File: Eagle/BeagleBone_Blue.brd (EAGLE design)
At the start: 86.4 x 54.6 mm, 297 parts, among them M1 JST_ZH_2, M2 JST_ZH_2, M3 JST_ZH_2, M4 JST_ZH_2, P10 SCHA5B0200, Q3 MOSFET-N, U1 TPD4S012_DRY_6, U4 TPD4S012_DRY_6, U5 24LC_32AT-I/OT, U6 SN74LVC1G07_DCK_5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

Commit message: Board and schematic consistent
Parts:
- C$1: value (none) -> AVE107M06D16T-F
- moved 6V_REG 207.4 mm to (-47.0, 63.5)
- moved ADC 207.4 mm to (-49.5, 88.9)
- moved BOOT 207.4 mm to (-29.2, 82.5)
- moved C1 207.4 mm to (-81.3, 109.2)
- moved C11 207.4 mm to (-80.0, 73.7)
- moved C13 207.4 mm to (-99.1, 109.2)
- moved C15 207.4 mm to (-104.1, 109.2)
- moved C17 207.4 mm to (-106.7, 109.2)
- moved C19 207.4 mm to (-14.0, 113.0)
- moved C22 207.4 mm to (-19.1, 113.0)
- moved C23 207.4 mm to (-90.2, 105.4)
- moved C24 207.4 mm to (-21.6, 113.0)
- moved C25 207.4 mm to (-94.0, 105.4)
- moved C26 207.4 mm to (-97.8, 105.4)
- moved C27 207.4 mm to (-24.1, 113.0)
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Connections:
- removed net BATT_MINUS1: BAL.5, BAL.6, C1.2, C15.1, C18.1, C19.2, LIPO.P$3, PROT.2, PROT.6, Q3.1, Q3.2, Q3.3
- removed net N$163: R152.2, R153.2, U7.2, U7.3
- new net BATT_MINUS: BAL.5, BAL.6, C1.2, C15.1, C18.1, C19.2, LIPO.P$3, PROT.2, PROT.6, Q3.1, Q3.2, Q3.3
- new net N$127: C$1.+, R152.2, R153.2, U7.2, U7.3
- net GND: now also C$1.-
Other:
- outline, holes or cut-outs redrawn

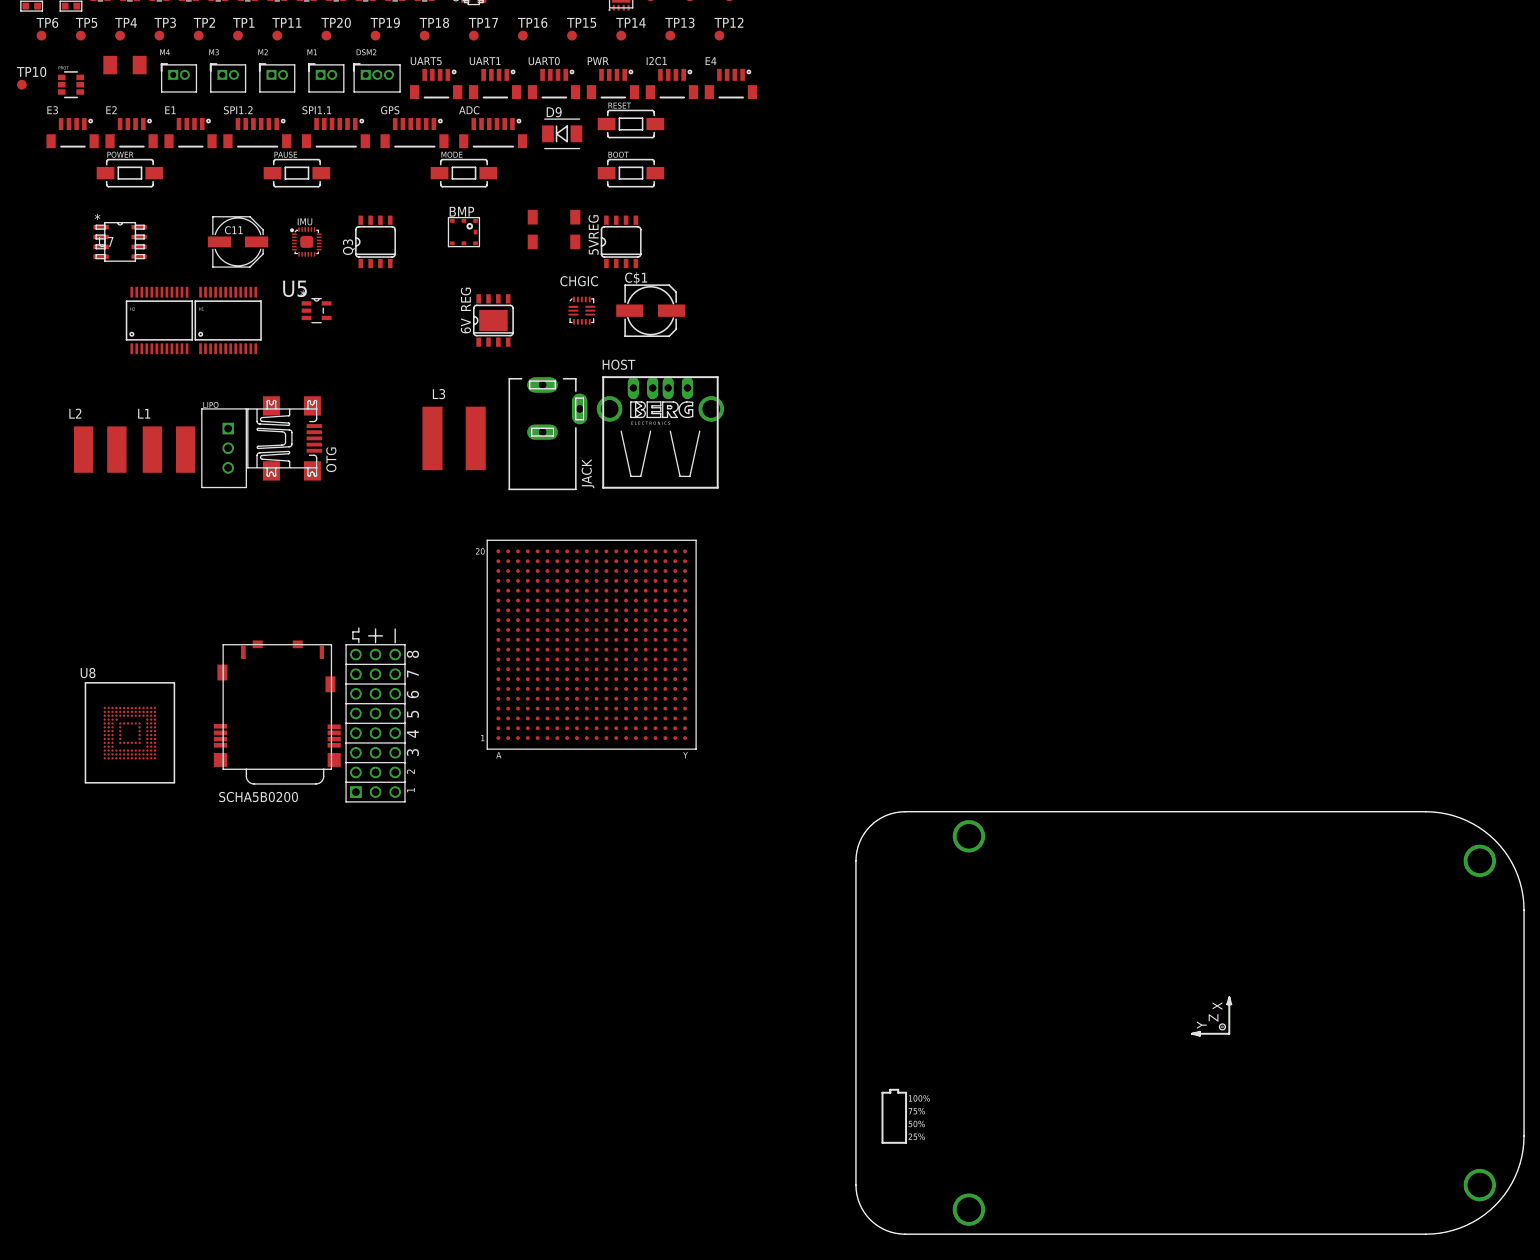
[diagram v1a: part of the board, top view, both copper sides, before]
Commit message: Spread a few components on the board
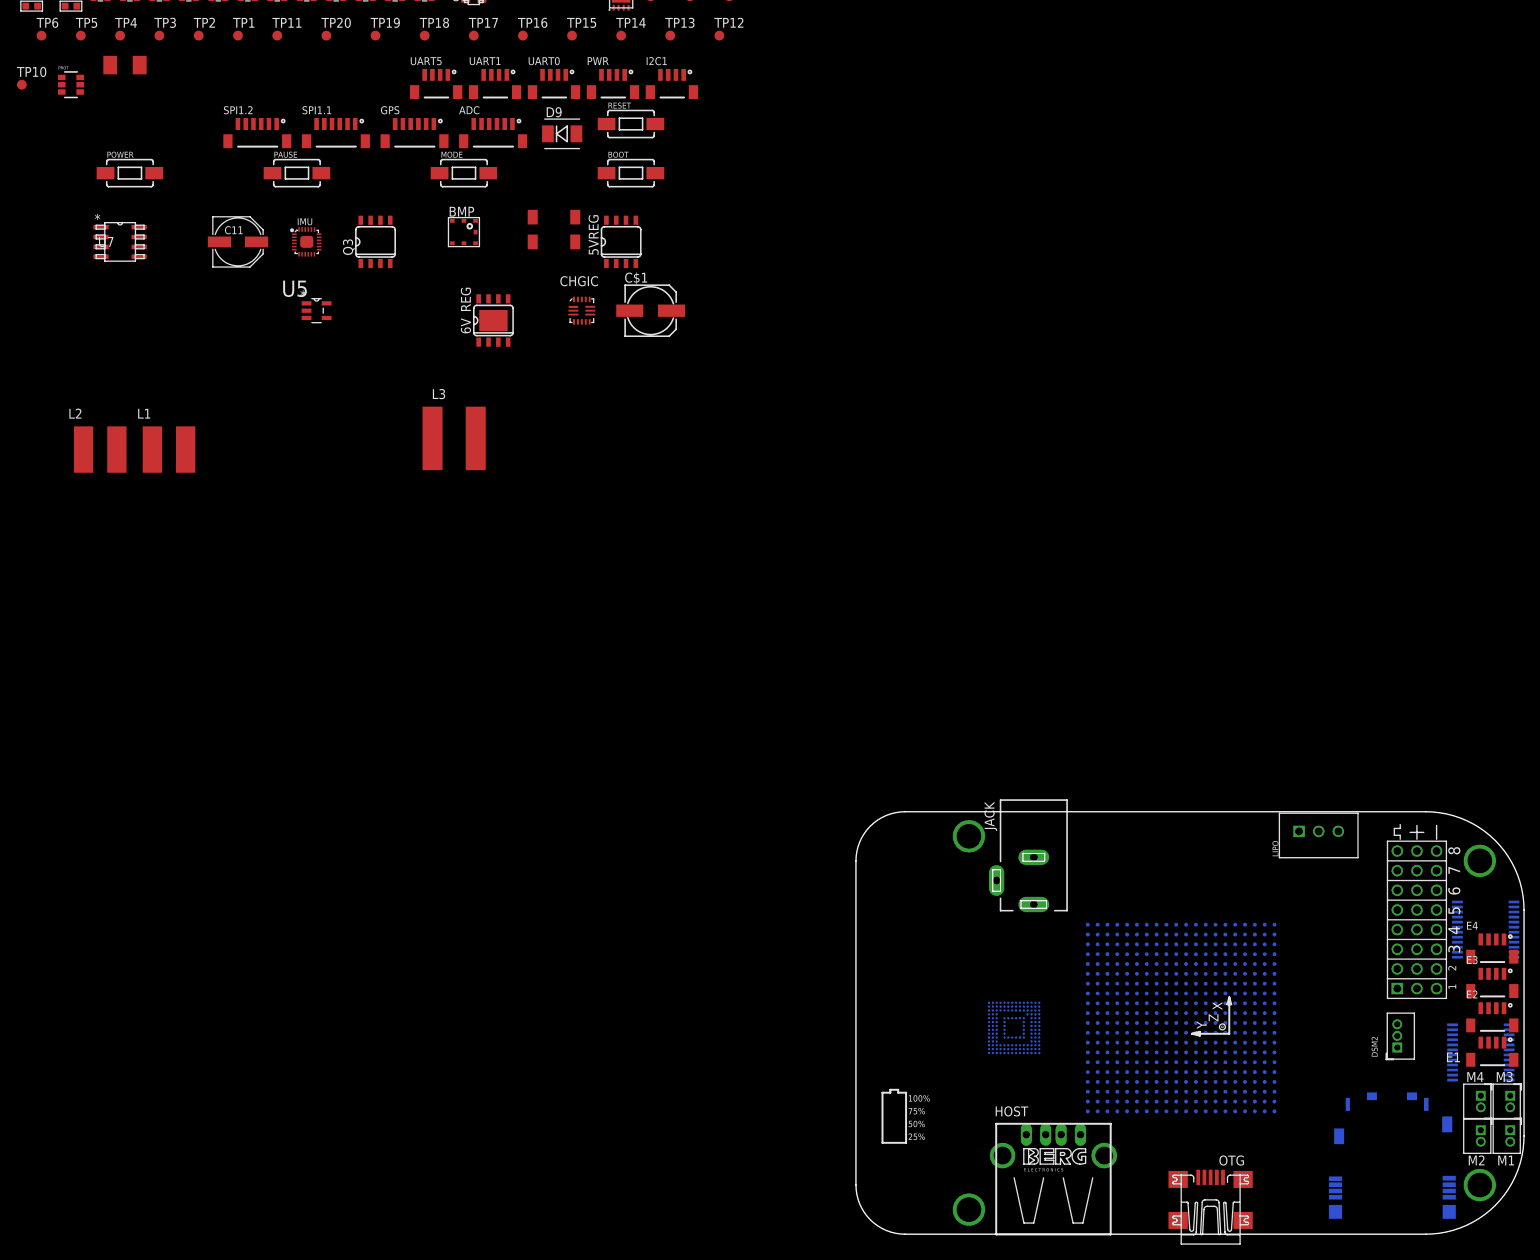
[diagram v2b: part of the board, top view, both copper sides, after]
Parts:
- moved M4 214.3 mm to (80.6, -37.5), turned to 270 degrees
- moved E3 213.9 mm to (83.2, -22.2)
- moved M3 212.3 mm to (84.5, -37.5), turned to 270 degrees
- moved E2 209.8 mm to (83.2, -26.7)
- moved M2 207.4 mm to (80.6, -41.9), turned to 270 degrees
- moved E1 206.0 mm to (83.2, -31.1)
- moved M1 205.5 mm to (84.5, -41.9), turned to 270 degrees
- moved H2 195.3 mm to (80.6, -31.1), flipped to the bottom, turned to 270 degrees
- moved DSM2 183.3 mm to (69.8, -30.5), turned to 90 degrees
- moved H1 180.6 mm to (81.3, -15.2), flipped to the bottom, turned to 270 degrees
- moved P10 176.9 mm to (80.6, -55.9), flipped to the bottom
- moved E4 148.9 mm to (83.2, -17.8)
- moved LIPO 147.9 mm to (57.1, -2.54), turned to 90 degrees
- moved U$1 137.0 mm to (72.4, -5.08)
- moved OTG 134.1 mm to (48.3, -35.6), turned to 90 degrees
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
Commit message: Connect MDIR_1A to pin C12
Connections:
- net MDIR_1A: now also SIP.C12
- net N$108: now also SIP.E17; no longer SIP.C12
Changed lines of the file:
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@@
 <signal name="MDIR_1A">
 <contactref element="H1" pad="21"/>
+<contactref element="SIP" pad="C12"/>
+<wire x1="40.005" y1="-17.145" x2="77.624" y2="-13.615" width="0" layer="19" extent="16-16"/>
 </signal>
 <signal name="MDIR_2A">
@@
 <wire x1="40.005" y1="-18.415" x2="-34.8488" y2="120.65" width="0" layer="19" extent="1-1"/>
 </signal>
-<signal name="N$108">
-<contactref element="SIP" pad="C12"/>
-<contactref element="R104" pad="1"/>
-<wire x1="40.005" y1="-17.145" x2="-37.3888" y2="120.65" width="0" layer="19" extent="1-1"/>
-</signal>
 <signal name="N$109">
 <contactref element="C36" pad="2"/>
@@
 <via x="80.518" y="-48.26" extent="1-16" drill="3.175"/>
 </signal>
+<signal name="N$108">
+<contactref element="R104" pad="1"/>
+<contactref element="SIP" pad="E17"/>
+<wire x1="33.655" y1="-19.685" x2="-37.3888" y2="120.65" width="0" layer="19" extent="1-16"/>
+</signal>
 </signals>

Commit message: Cleared all errors
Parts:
- 5VREG: device Strawson_Eagle_Lib:SO08-TIGHT -> BeagleBone_Blue:SO08-TIGHT
- moved 5VREG 151.8 mm to (-113.7, -53.3)

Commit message: Cleared all warnings
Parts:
- L4, L5: value (none) -> 120
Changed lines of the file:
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@@
 </element>
 <element name="L3" library="Strawson_Eagle_Lib" package="8X8MM_INDUCTOR" value="3.6" x="-52.07" y="48.26"/>
-<element name="L4" library="Seeed-OPL-Inductor" package="L0603" value="" x="-101.6" y="104.14"/>
-<element name="L5" library="Seeed-OPL-Inductor" package="L0603" value="" x="-106.68" y="104.14"/>
+<element name="L4" library="Seeed-OPL-Inductor" package="L0603" value="120" x="-101.6" y="104.14"/>
+<element name="L5" library="Seeed-OPL-Inductor" package="L0603" value="120" x="-106.68" y="104.14"/>
 <element name="LIPO" library="Strawson_Eagle_Lib" package="JST_XH_3-PIN" value="" x="57.15" y="-2.54" rot="R90"/>
 <element name="M1" library="Strawson_Eagle_Lib" package="JST_ZH_2" value="JST_ZH_2" x="84.455" y="-41.91" smashed="yes" rot="R270">

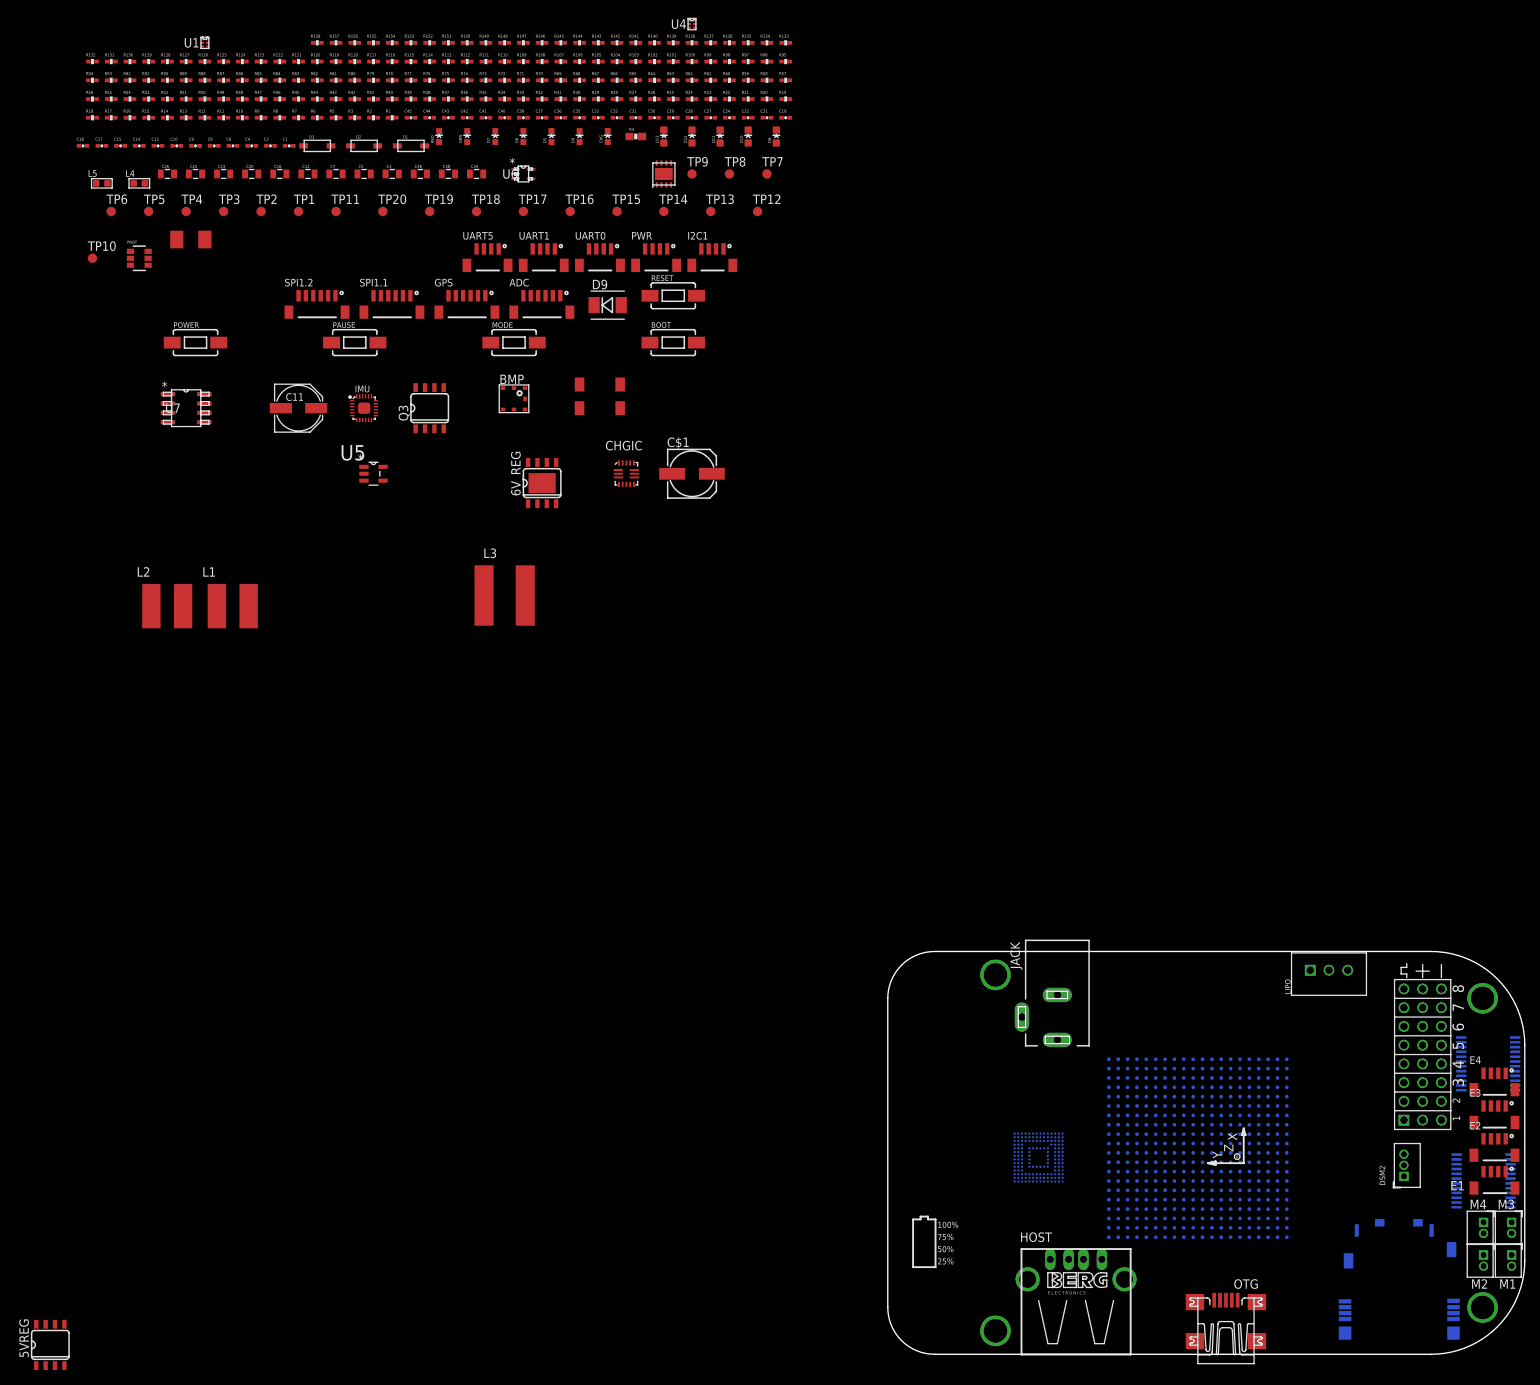
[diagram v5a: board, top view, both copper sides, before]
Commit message: Rough placed a bunch of parts
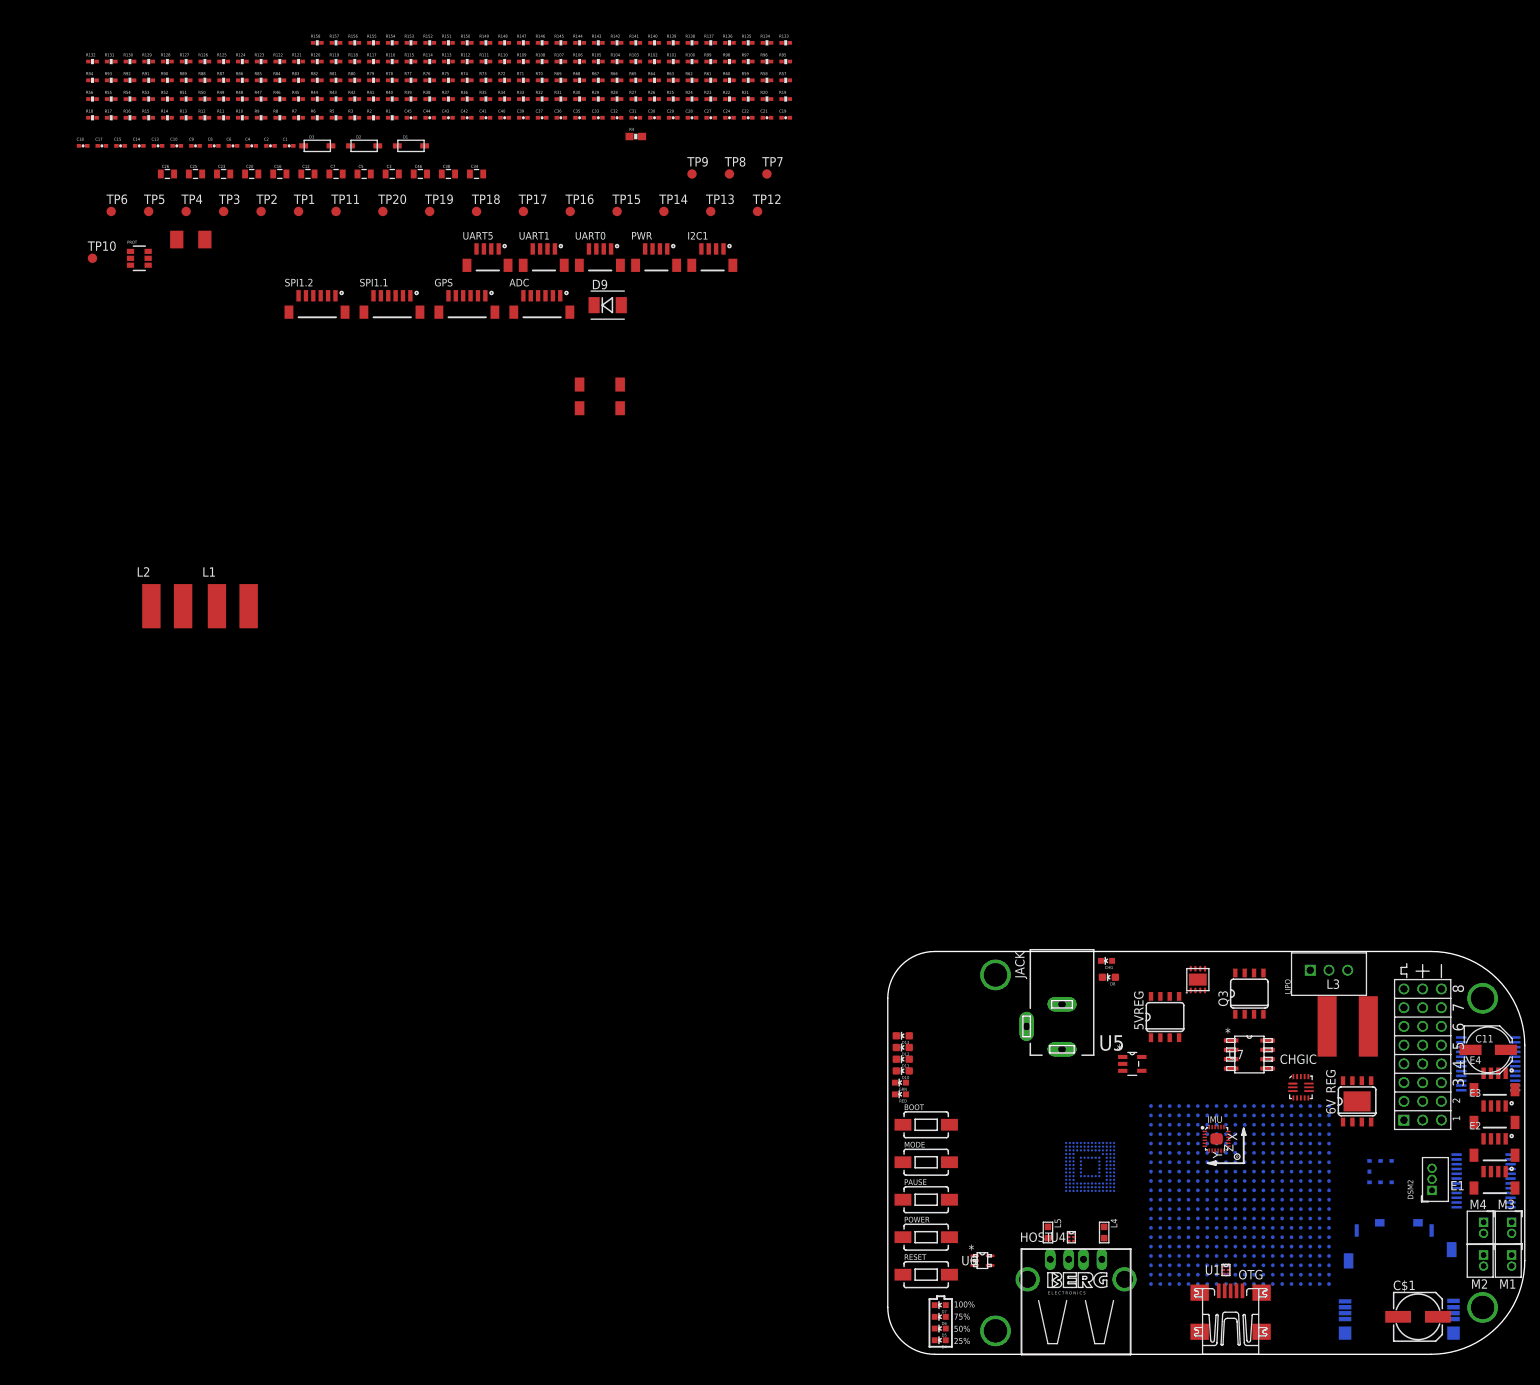
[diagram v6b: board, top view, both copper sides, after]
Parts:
- moved U1 216.4 mm to (45.7, -43.2)
- moved L4 193.2 mm to (29.2, -38.1), turned to 270 degrees
- moved L5 191.5 mm to (21.6, -38.1), turned to 270 degrees
- moved C11 183.3 mm to (81.3, -13.3)
- moved U4 172.3 mm to (24.8, -38.7)
- moved D4 170.4 mm to (6.99, -52.7), turned to 90 degrees
- moved D5 170.0 mm to (6.99, -51.1), turned to 90 degrees
- moved D6 169.7 mm to (6.99, -49.5), turned to 90 degrees
- moved D7 169.5 mm to (6.99, -47.9), turned to 90 degrees
- moved U7 168.7 mm to (48.9, -14.0)
- moved U6 159.9 mm to (12.7, -41.9)
- moved 5VREG 157.5 mm to (37.5, -8.89)
- moved BMP 157.4 mm to (66.7, -29.8), flipped to the bottom
- moved POWER 156.6 mm to (5.08, -38.7)
- moved IMU 152.2 mm to (44.5, -25.4)
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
